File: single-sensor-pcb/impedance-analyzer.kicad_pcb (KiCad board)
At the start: 2 copper layers, 61.9 x 56.5 mm, 11 parts, among them J1 AD9833, J2 ADS1256_SPI, J3 ADS1256_AIN, J4 UNO_POWER, J5 UNO_ANALOG, J6 UNO_DIGITAL_LOW, J7 UNO_DIGITAL_HIGH, J8 PIEZO

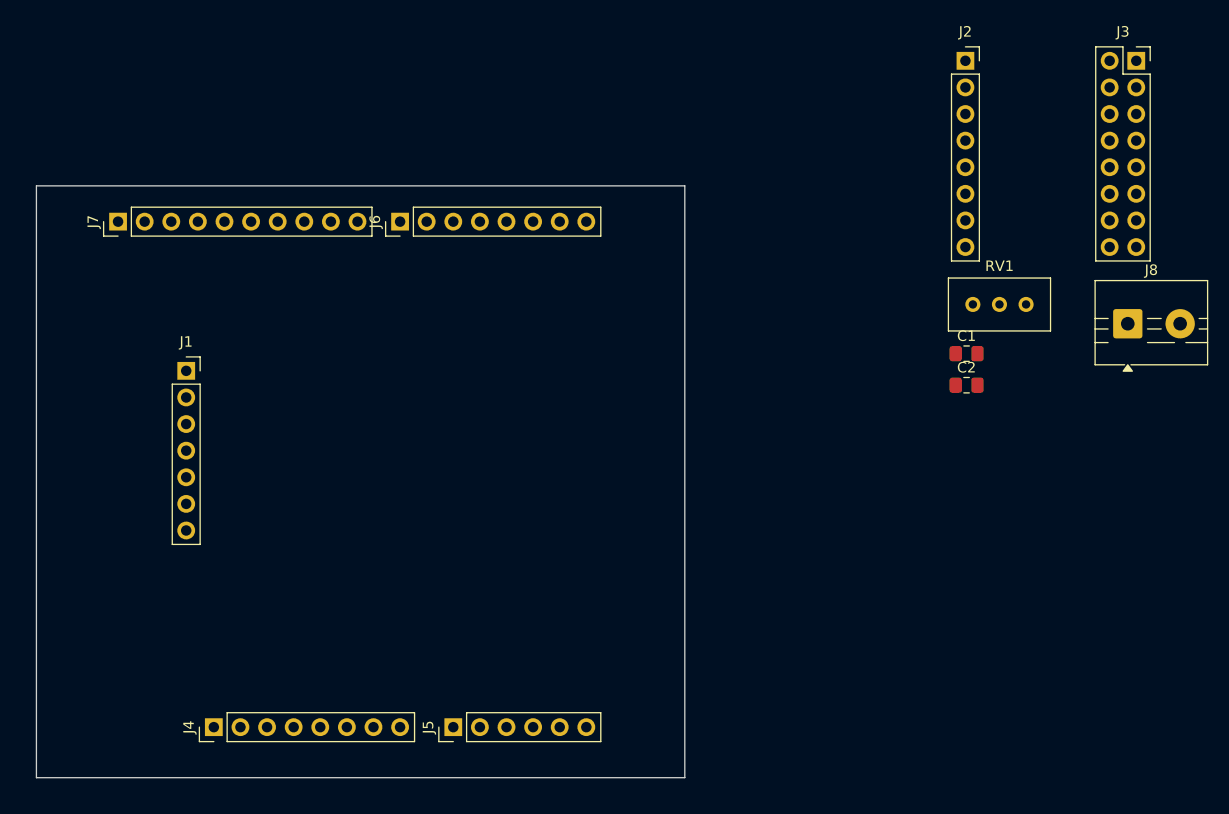
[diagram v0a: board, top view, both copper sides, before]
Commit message: routed single sensor board, drc clean
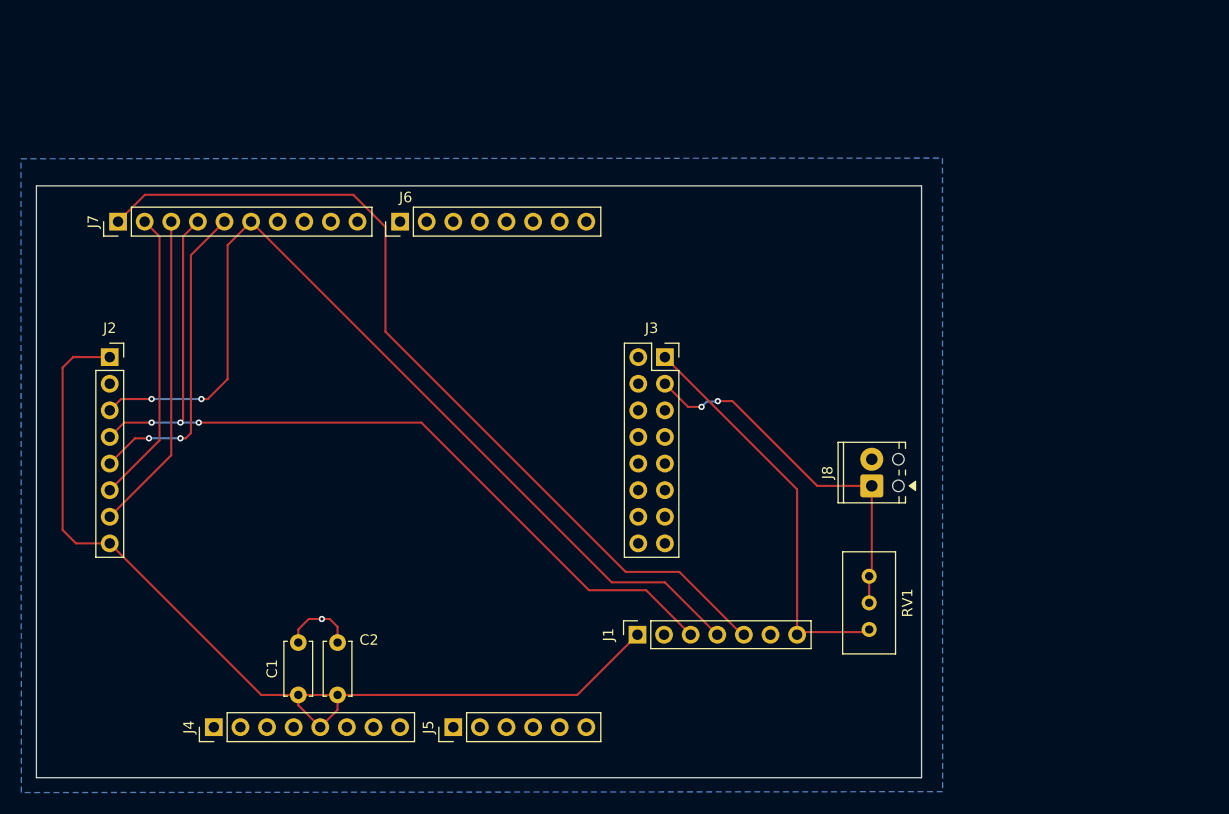
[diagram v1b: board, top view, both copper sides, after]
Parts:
- C1, C2: footprint Capacitor_SMD:C_0805_2012Metric_Pad1.18x1.45mm_HandSolder -> Capacitor_THT:C_Disc_D5.0mm_W2.5mm_P5.00mm
- J8: footprint TerminalBlock:TerminalBlock_MaiXu_MX126-5.0-02P_1x02_P5.00mm -> TerminalBlock_Phoenix:TerminalBlock_Phoenix_MPT-0,5-2-2.54_1x02_P2.54mm_Horizontal
- moved J2 86.4 mm to (129.0, 88.5)
- moved C1 71.6 mm to (147.0, 120.8), turned to 90 degrees
- moved C2 66.9 mm to (150.8, 120.8), turned to 90 degrees
- moved J3 53.2 mm to (182.0, 88.5)
- moved J1 49.9 mm to (179.4, 115.0), turned to 90 degrees
- moved RV1 34.5 mm to (201.5, 114.5), turned to -90 degrees
- moved J8 28.9 mm to (201.8, 100.8), turned to 90 degrees
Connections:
- J3 pad 10: unconnected-(J3-Pin_10-Pad10) -> GND
- J3 pad 11: unconnected-(J3-Pin_11-Pad11) -> GND
- J3 pad 12: unconnected-(J3-Pin_12-Pad12) -> GND
- J3 pad 13: unconnected-(J3-Pin_13-Pad13) -> GND
- J3 pad 14: unconnected-(J3-Pin_14-Pad14) -> GND
- J3 pad 5: unconnected-(J3-Pin_5-Pad5) -> GND
- J3 pad 6: unconnected-(J3-Pin_6-Pad6) -> GND
- J3 pad 7: unconnected-(J3-Pin_7-Pad7) -> GND
- J3 pad 8: unconnected-(J3-Pin_8-Pad8) -> GND
- J3 pad 9: unconnected-(J3-Pin_9-Pad9) -> GND
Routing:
- net +5V: track 0.00 -> 91.9 mm
- net SCLK: track 0.00 -> 89.3 mm, vias 0 -> 2
- net SDATA: track 0.00 -> 84.3 mm, vias 0 -> 3
- net FSYNC: track 0.00 -> 84.1 mm
- net AD9833_OUT: track 0.00 -> 38.8 mm
- net VMID_NODE: track 0.00 -> 35.5 mm, vias 0 -> 2
- net ADC_CS: track 0.00 -> 30.6 mm
- net MISO: track 0.00 -> 30.5 mm, vias 0 -> 2
- net DRDY: track 0.00 -> 28.2 mm
- net GND: track 0.00 -> 7.22 mm, vias 0 -> 1
- added copper zone on B.Cu, net GND
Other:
- board size 61.9 x 56.5 mm -> 84.5 x 56.5 mm
